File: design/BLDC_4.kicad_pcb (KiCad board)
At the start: 4 copper layers, 38.5 x 65 mm, 127 parts, among them K1 SERVO, P1 HALL/Encoder, P101 CANBUS, P2 SWD, P3 PWR_COMM, P4 IN+, P5 IN-, P6 MOTOR1, P7 MOTOR2, P9 MOTOR3, Q1 IRFS7530, Q2 IRFS7530, Q3 IRFS7530, Q4 IRFS7530, Q5 IRFS7530, Q6 IRFS7530, U1 STM32F40X_LQFP64, U2 TC2117, U3 DRV8302, U401 SN65HVD232, X1 MINI-USB-SHIELD-32005-201, X2 8MHz 10ppm

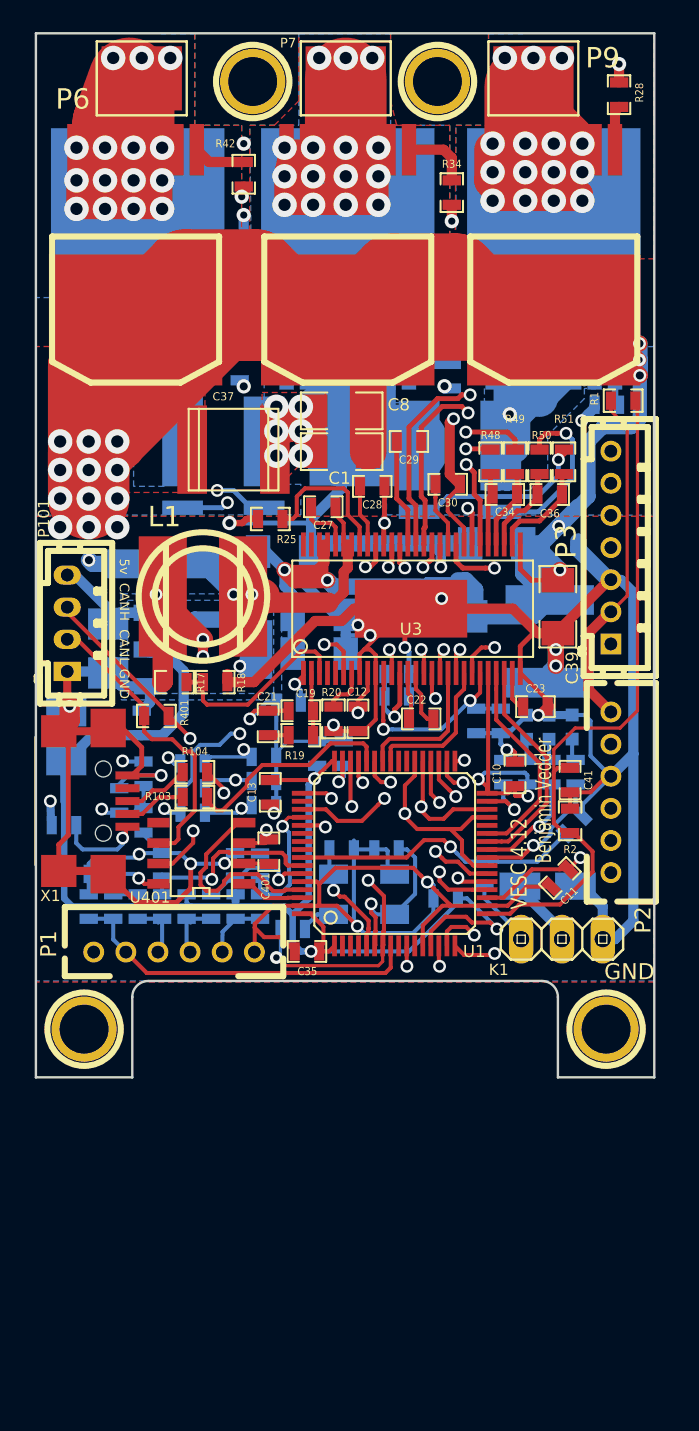
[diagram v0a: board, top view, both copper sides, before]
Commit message: added usb connector
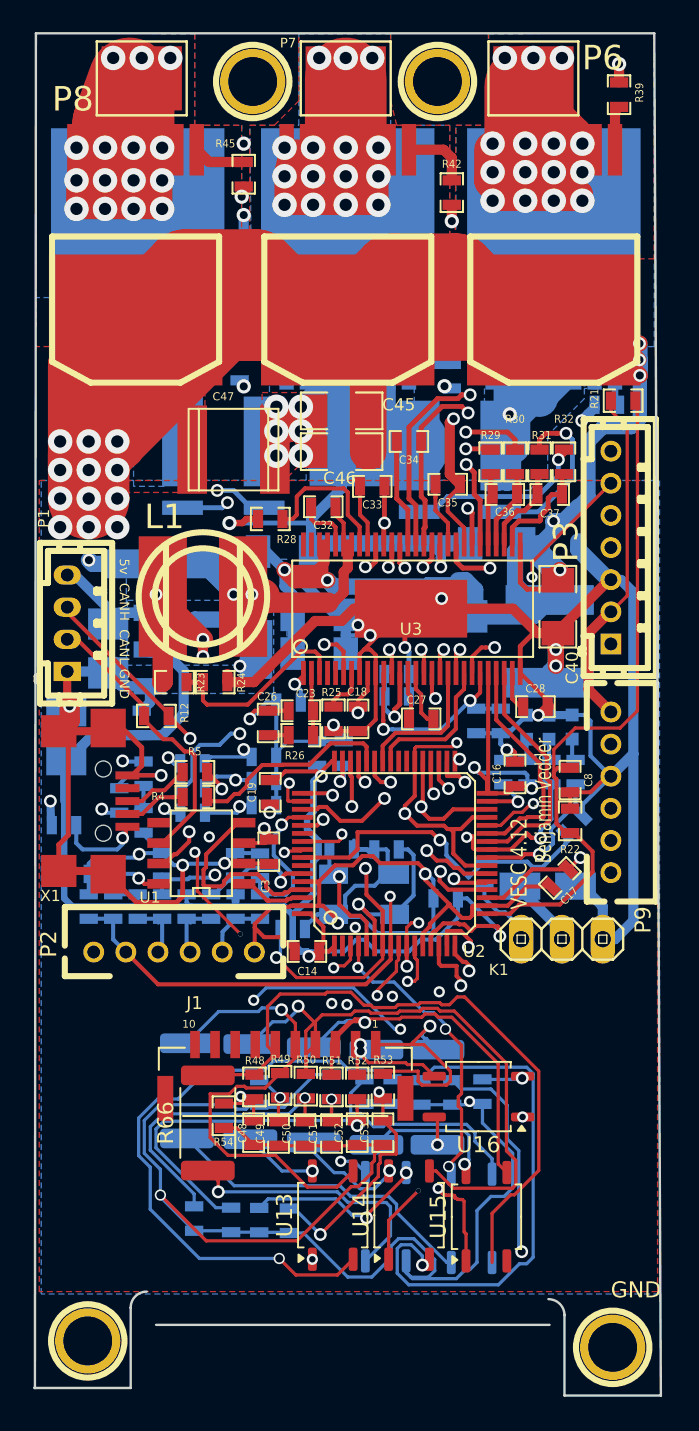
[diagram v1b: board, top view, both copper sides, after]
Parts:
- added C48: 100n, CRF1:SMD-0603_c, F.Cu at (92.1, 148.4)
- added C49: 100n, CRF1:SMD-0603_c, F.Cu at (93.6, 148.5)
- added C50: 100n, CRF1:SMD-0603_c, F.Cu at (95.3, 148.5)
- added C51: 100n, CRF1:SMD-0603_c, F.Cu at (96.9, 148.5)
- added C52: 100n, CRF1:SMD-0603_c, F.Cu at (98.5, 148.4)
- added C53: 100n, CRF1:SMD-0603_c, F.Cu at (100.1, 148.4)
- added J1: BM10B-GHS-TBT_LF__SN__N_, jst-gh:JST_BM10B-GHS-TBT_LF__SN__N_, F.Cu at (94.0, 145.3)
- added R48: 18k, CRF1:SMD-0603_r, F.Cu at (92.1, 145.6)
- added R49: 18k, CRF1:SMD-0603_r, F.Cu at (93.7, 145.5)
- added R50: 18k, CRF1:SMD-0603_r, F.Cu at (95.3, 145.5)
- added R51: 18k, CRF1:SMD-0603_r, F.Cu at (96.9, 145.6)
- added R52: 18k, CRF1:SMD-0603_r, F.Cu at (98.5, 145.6)
- added R53: 18k, CRF1:SMD-0603_r, F.Cu at (100.1, 145.5)
- added R54: 2k2, CRF1:SMD-0603_r, F.Cu at (90.2, 147.4)
- added R55: 2k2, CRF1:SMD-0603_r, B.Cu at (92.4, 145.9)
- added R56: 2k2, CRF1:SMD-0603_r, B.Cu at (88.4, 153.8)
- added R57: 2k2, CRF1:SMD-0603_r, B.Cu at (96.9, 145.6)
- added R58: 2k2, CRF1:SMD-0603_r, B.Cu at (90.7, 153.9)
- added R59: 2k2, CRF1:SMD-0603_r, B.Cu at (94.3, 153.9)
- added R60: 360, CRF1:SMD-0603_r, B.Cu at (92.4, 153.9)
- added R61: 360, CRF1:SMD-0603_r, B.Cu at (99.0, 145.9)
- added R62: 360, CRF1:SMD-0603_r, B.Cu at (100.7, 145.9)
- added R63: 360, CRF1:SMD-0603_r, B.Cu at (102.5, 145.9)
- added R64: 360, CRF1:SMD-0603_r, B.Cu at (104.4, 145.9)
- added R65: 360, CRF1:SMD-0603_r, B.Cu at (106.3, 145.9)
- added R66: 16, Resistor_SMD:R_2512_6332Metric, F.Cu at (89.2, 147.8)
- added R67: 16, Resistor_SMD:R_2512_6332Metric, B.Cu at (87.9, 145.8)
- added R68: 16, Resistor_SMD:R_2512_6332Metric, B.Cu at (91.9, 145.9)
- added R69: 16, Resistor_SMD:R_2512_6332Metric, B.Cu at (95.8, 146.1)
- added R70: 16, Resistor_SMD:R_2512_6332Metric, B.Cu at (99.7, 146.2)
- added R71: 16, Resistor_SMD:R_2512_6332Metric, B.Cu at (103.5, 146.2)
- added U11: CPC1002N, Package_SO:SOP-4_3.8x4.1mm_P2.54mm, B.Cu at (100.3, 153.7)
- added U12: CPC1002N, Package_SO:SOP-4_3.8x4.1mm_P2.54mm, B.Cu at (105.6, 153.8)
- added U13: CPC1002N, Package_SO:SOP-4_3.8x4.1mm_P2.54mm, F.Cu at (97.0, 153.6)
- added U14: CPC1002N, Package_SO:SOP-4_3.8x4.1mm_P2.54mm, F.Cu at (101.7, 153.6)
- added U15: CPC1002N, Package_SO:SOP-4_3.8x4.1mm_P2.54mm, F.Cu at (106.6, 153.7)
- added U16: CPC1002N, Package_SO:SOP-4_3.8x4.1mm_P2.54mm, F.Cu at (106.1, 146.2)
- moved 1PIN 19.8 mm to (114.4, 161.8)
- moved 1PIN 19.4 mm to (81.7, 161.4)
- renumbered C2 to C1, C16 to C10, C17 to C11, C31 to C12, C32 to C13, C35 to C14, C38 to C15, C10 to C16, C11 to C17, C12 to C18, C13 to C19, C3 to C2, C14 to C20, C26 to C21, C18 to C22, C19 to C23, C52 to C24, C20 to C25, C21 to C26, C22 to C27, C23 to C28, C43 to C29, C401 to C3, C44 to C30, C49 to C31, C27 to C32, C28 to C33, C29 to C34, C30 to C35, C34 to C36, C36 to C37, C24 to C38, C25 to C39, C39 to C40, C33 to C41, C9 to C42, C40 to C43, C51 to C44, C8 to C45, C1 to C46, C37 to C47, C41 to C8, C15 to C9, D2 to D1, D1 to D2, P101 to P1, P1 to P2, P9 to P6, P6 to P8, P2 to P9, R3 to R1, R54 to R10, R53 to R11, R401 to R12, R402 to R13, R7 to R14, R11 to R15, R12 to R16, R13 to R17, R10 to R18, R9 to R19, R4 to R2, R8 to R20, R1 to R21, R2 to R22, R17 to R23, R18 to R24, R20 to R25, R19 to R26, R21 to R27, R25 to R28, R48 to R29, R6 to R3, R49 to R30, R50 to R31, R51 to R32, R23 to R33, R24 to R34, R26 to R35, R27 to R36, R32 to R37, R33 to R38, R28 to R39, R103 to R4, R29 to R40, R30 to R41, R34 to R42, R35 to R43, R36 to R44, R42 to R45, R43 to R46, R46 to R47, R104 to R5, R38 to R6, R37 to R7, R22 to R8, R5 to R9, U401 to U1, U1 to U2, U2 to U4
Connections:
- net /MCU/MISO_ADC_EXT2 renamed /MISO_RX_SCL
- net /MCU/SCK_ADC_EXT renamed /SCK_ADC_EXT
- C4 pad 2: /Filters/TEMP_IN -> /Filters/TEMP_MOTOR
- P2 pad 2: /Filters/TEMP_IN -> /Filters/TEMP_MOTOR
- P3 pad 5: /MCU/TX_SDA_NSS -> /TX_SDA
- P3 pad 6: /MCU/RX_SCL_MOSI -> /RX_SCL_MOSI
- P9 pad 6: Net-(P2-Pad6) -> unconnected-(P9-Pad6)
- R14 pad 1: /Filters/TEMP_IN -> /Filters/TEMP_MOTOR
- U1 pad 5: Net-(U401-Pad5) -> unconnected-(U1-Vref-Pad5)
- U2 pad 10: /MCU/AN_IN -> /Battery voltage control/Cell3_ADC
- U2 pad 11: Net-(U1-Pad11) -> /Battery voltage control/Cell4_ADC
- U2 pad 2: Net-(U1-Pad2) -> /RX_SCL_MOSI
- U2 pad 20: /MCU/TX_SDA_NSS -> /Filters/TEMP_MOTOR
- U2 pad 23: /MCU/RX_SCL_MOSI -> /MCU/AN_IN
- U2 pad 24: /MCU/LED_GREEN -> /Battery voltage control/Cell5_ADC
- U2 pad 25: /MCU/LED_RED -> /Battery voltage control/Cell6_ADC
- U2 pad 28: Net-(U1-Pad28) -> /Battery voltage control/Cell4_control
- U2 pad 29: /MCU/RX_SCL_MOSI -> /RX_SCL_MOSI
- U2 pad 3: Net-(U1-Pad3) -> /Battery voltage control/Cell6_control
- U2 pad 30: /MCU/TX_SDA_NSS -> /TX_SDA
- U2 pad 37: /MCU/TX_SDA_NSS -> /TX_SDA
- U2 pad 38: /MCU/RX_SCL_MOSI -> /RX_SCL_MOSI
- U2 pad 39: Net-(U1-Pad39) -> /MCU/LED_GREEN
- U2 pad 4: Net-(U1-Pad4) -> /Battery voltage control/Cell5_control
- U2 pad 40: Net-(U1-Pad40) -> /MCU/LED_RED
- U2 pad 50: Net-(U1-Pad50) -> /Battery voltage control/Cell3_control
- U2 pad 54: Net-(U1-Pad54) -> /TX_SDA
- U2 pad 55: Net-(U1-Pad55) -> /Battery voltage control/Cell2_control
- U2 pad 56: Net-(U1-Pad56) -> /Battery voltage control/Cell1_control
- U2 pad 8: /Filters/TEMP_IN -> /Battery voltage control/Cell1_ADC
- U2 pad 9: Net-(U1-Pad9) -> /Battery voltage control/Cell2_ADC
- U3 pad 4: Net-(U3-Pad4) -> unconnected-(U3-PWRGD-Pad4)
- U3 pad 5: Net-(U3-Pad5) -> unconnected-(U3-OCTW-Pad5)
- U3 pad 55: Net-(U3-Pad55) -> unconnected-(U3-EN_BUCK-Pad55)
- U3 pad 56: Net-(U3-Pad56) -> unconnected-(U3-SS_TR-Pad56)
- X1 pad 4: Net-(X1-Pad4) -> unconnected-(X1-Pad4)
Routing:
- net GND: track 398.8 -> 517.8 mm, vias 27 -> 30
- net (no net): track 0.00 -> 70.1 mm, vias 0 -> 2
- net /Battery voltage control/Cell3_control: track 0.00 -> 47.7 mm, vias 0 -> 6
- net /MCU/TX_SDA_NSS: track 47.1 -> 0.00 mm, vias 2 -> 0
- net /MCU/AN_IN: track 28.9 -> 72.1 mm, vias 2 -> 3
- net /Battery voltage control/Cell1_control: track 0.00 -> 42.4 mm, vias 0 -> 4
- net /Battery voltage control/Cell6: track 0.00 -> 41.7 mm
- net /MCU/RX_SCL_MOSI: track 41.6 -> 0.00 mm, vias 1 -> 0
- net /Battery voltage control/Cell4_control: track 0.00 -> 40.4 mm, vias 0 -> 2
- net /Battery voltage control/Cell4: track 0.00 -> 40.1 mm, vias 0 -> 1
- net Net-(R62-Pad1): track 0.00 -> 38.5 mm, vias 0 -> 1
- net /Battery voltage control/Cell6_ADC: track 0.00 -> 37.5 mm, vias 0 -> 3
- net /Battery voltage control/Cell2_control: track 0.00 -> 37.5 mm, vias 0 -> 2
- net /Battery voltage control/Cell2_ADC: track 0.00 -> 35.1 mm, vias 0 -> 2
- net /Battery voltage control/Cell1_ADC: track 0.00 -> 34.1 mm, vias 0 -> 4
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- added copper zone on In1.Cu, net /Mosfet driver/H1_VS
- added copper zone on In2.Cu, net /Mosfet driver/H1_VS
- added copper zone on In1.Cu, net /Mosfet driver/H2_VS
- added copper zone on In2.Cu, net /Mosfet driver/H2_VS
- added copper zone on In1.Cu, net /Mosfet driver/H3_VS
- added copper zone on In2.Cu, net /Mosfet driver/H3_VS
- added copper zone on In1.Cu, net GND
- added copper zone on In2.Cu, net GND
- removed copper zone on GND, net /Mosfet driver/H1_VS
- removed copper zone on GND2, net /Mosfet driver/H1_VS
- removed copper zone on GND, net /Mosfet driver/H2_VS
- removed copper zone on GND2, net /Mosfet driver/H2_VS
- removed copper zone on GND, net /Mosfet driver/H3_VS
- removed copper zone on GND2, net /Mosfet driver/H3_VS
- removed copper zone on GND, net GND
- removed copper zone on GND2, net GND
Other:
- board size 38.5 x 65 mm -> 39 x 84.8 mm
- net class Default removed

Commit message: started pcb tracing
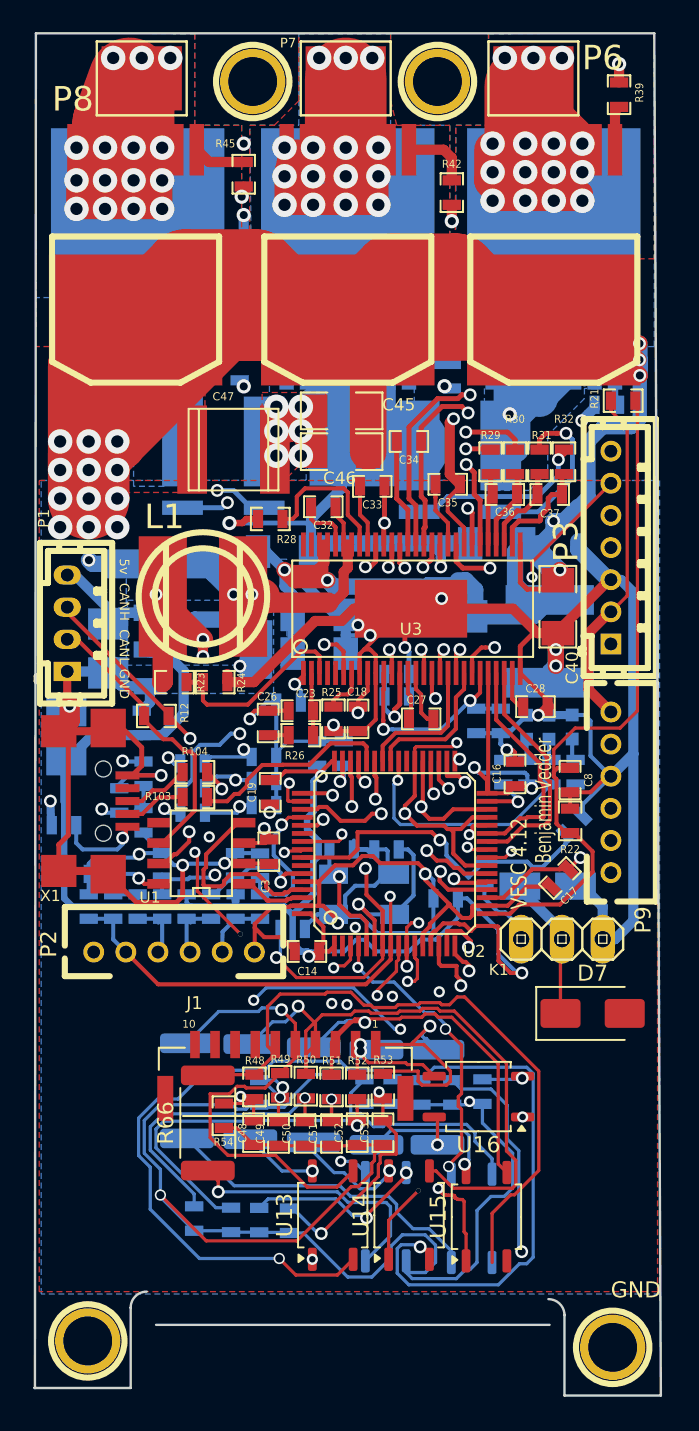
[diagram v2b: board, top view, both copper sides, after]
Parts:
- added D7: SS24, Diode_SMD:D_SMA, F.Cu at (113.2, 141.0)
- R103: renamed from R4; value 22R -> 5k1
- R104: renamed from R5; value 22R -> 5k1
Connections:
- R103 pad 1: /MCU/USB_DM -> GND
- R103 pad 2: Net-(R4-Pad2) -> Net-(J2-CC2)
- R104 pad 1: /MCU/USB_DP -> GND
- R104 pad 2: Net-(R5-Pad2) -> Net-(J2-CC1)
- U2 pad 44: /MCU/USB_DM -> /MCU/USB_C_D-
- U2 pad 45: /MCU/USB_DP -> /MCU/USB_C_D+
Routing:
- net /Battery voltage control/Cell5_ADC: track 3.27 -> 53.7 mm, vias 1 -> 3
- net GND: track 517.8 -> 544.0 mm, vias 30 -> 32
- net /MCU/USB_DP: track 13.2 -> 0.00 mm, vias 2 -> 0
- net /MCU/USB_DM: track 12.7 -> 0.00 mm
- net VCC: track 192.0 -> 201.4 mm
- net /MCU/LED_GREEN: track 8.84 -> 0.00 mm, vias 1 -> 0
- net /MCU/LED_RED: track 7.50 -> 14.7 mm
- net /Battery voltage control/Cell6_ADC: track 37.5 -> 30.4 mm
- net +5V: track 115.7 -> 120.4 mm
- net /Battery voltage control/Cell4_control: track 40.4 -> 35.8 mm
- net /MCU/H1: track 10.1 -> 12.1 mm
- net Net-(R63-Pad1): track 32.4 -> 31.5 mm
- net SWDIO: track 25.0 -> 25.7 mm
- net SWCLK: track 25.6 -> 26.2 mm
- net /MCU/EN_GATE: track 19.8 -> 20.3 mm

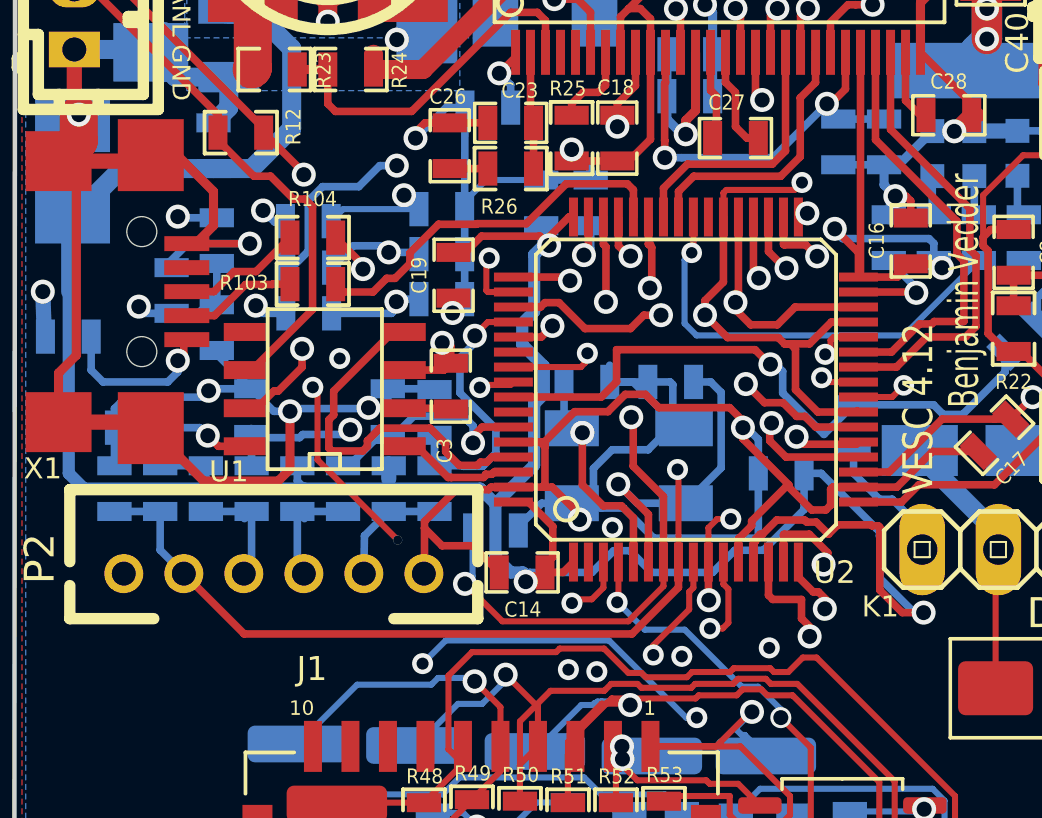
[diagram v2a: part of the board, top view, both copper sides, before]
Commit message: added new field in components on battery balancer; pcb tracing
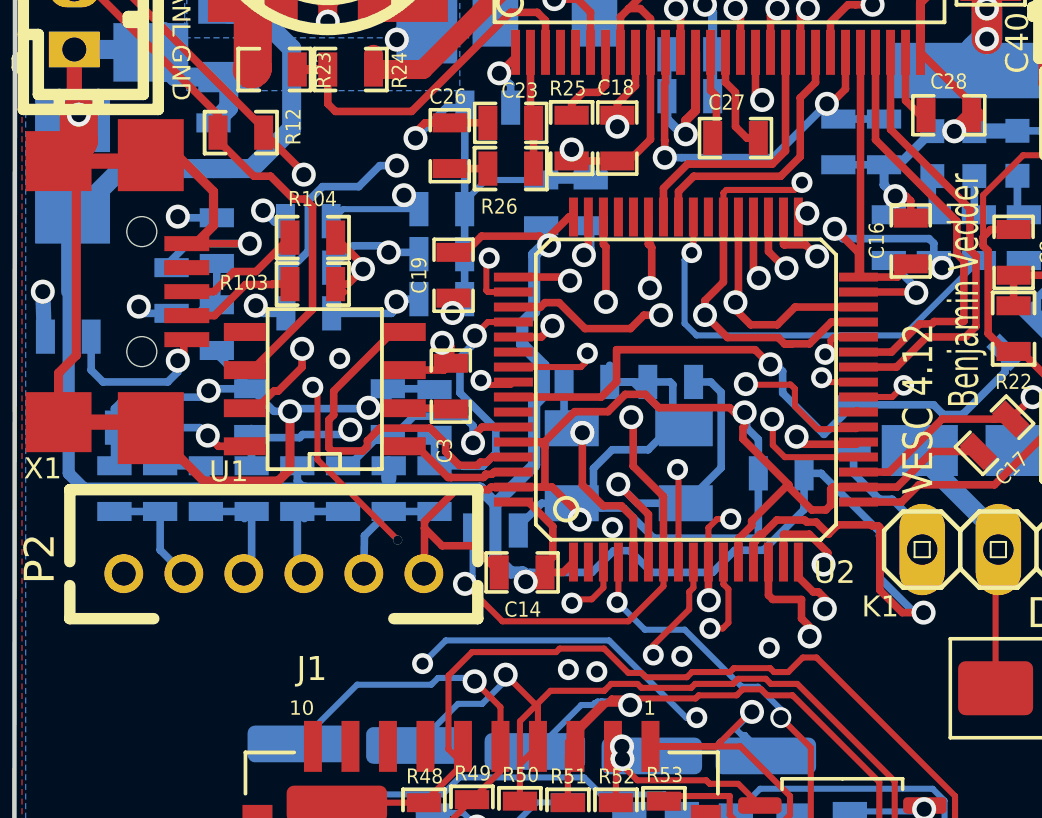
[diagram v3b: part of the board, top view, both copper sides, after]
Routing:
- net (no net): track 70.1 -> 0.00 mm, vias 2 -> 0
- net /MCU/AN_IN: track 72.1 -> 30.3 mm, vias 3 -> 2
- net /Filters/TEMP_MOTOR: track 0.00 -> 40.6 mm, vias 0 -> 1
- net /TX_SDA: track 0.00 -> 39.3 mm, vias 0 -> 1
- net /RX_SCL_MOSI: track 23.3 -> 61.1 mm, vias 2 -> 3
- net GND: track 544.0 -> 529.1 mm, vias 32 -> 31
- net /MCU/SENS1: track 5.39 -> 6.36 mm

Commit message: added documentation
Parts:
- moved 1PIN 0.69 mm to (81.5, 162.0)
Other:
- board size 39 x 84.8 mm -> 39 x 85 mm
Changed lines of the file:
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@@
 		(tenting front back)
 		(pcbplotparams
-			(layerselection 0x00000000_00000000_00000000_0200a0ff)
+			(layerselection 0x00000000_00000000_55555555_55555525)
 			(plot_on_all_layers_selection 0x00000000_00000000_00000000_00000000)
 			(disableapertmacros no)
@@
 			(crossoutdnponfab yes)
 			(subtractmaskfromsilk yes)
-			(outputformat 1)
+			(outputformat 3)
 			(mirror no)
 			(drillshape 0)
@@
 	(footprint "Connect:1pin"
 		(layer "F.Cu")
-		(at 81.73 161.41)
+		(at 81.45 162.04)
 		(descr "module 1 pin (ou trou mecanique de percage)")
 		(tags "DEV")
@@
 	)
 	(gr_line
-		(start 85.98 160.41)
-		(end 110.48 160.41)
+		(start 85.42 158.95)
+		(end 110.41 158.81)
 		(stroke
 			(width 0.15)
@@
 	)
 	(gr_line
-		(start 78.44 164.35)
+		(start 78.44 164.97)
 		(end 78.5 80)
 		(stroke
@@
 	)
 	(gr_line
-		(start 84.4 159.34)
-		(end 84.4 164.34)
+		(start 84.42 159.95)
+		(end 84.42 164.95)
 		(stroke
 			(width 0.15)
@@
 	)
 	(gr_arc
-		(start 84.4 159.34)
-		(mid 84.692893 158.632893)
-		(end 85.4 158.34)
+		(start 84.42 159.95)
+		(mid 84.712893 159.242893)
+		(end 85.42 158.95)
 		(stroke
 			(width 0.15)
@@
 	)
 	(gr_line
-		(start 84.4 164.34)
-		(end 78.4 164.34)
+		(start 84.42 164.95)
+		(end 78.44 164.97)
 		(stroke
 			(width 0.15)
